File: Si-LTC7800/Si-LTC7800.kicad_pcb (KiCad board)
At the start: 2 copper layers, 40 parts, among them Q1 BSC100N06LS3_G, Q2 BSC100N06LS3_G, U1 LTC7800HUDC_PBF

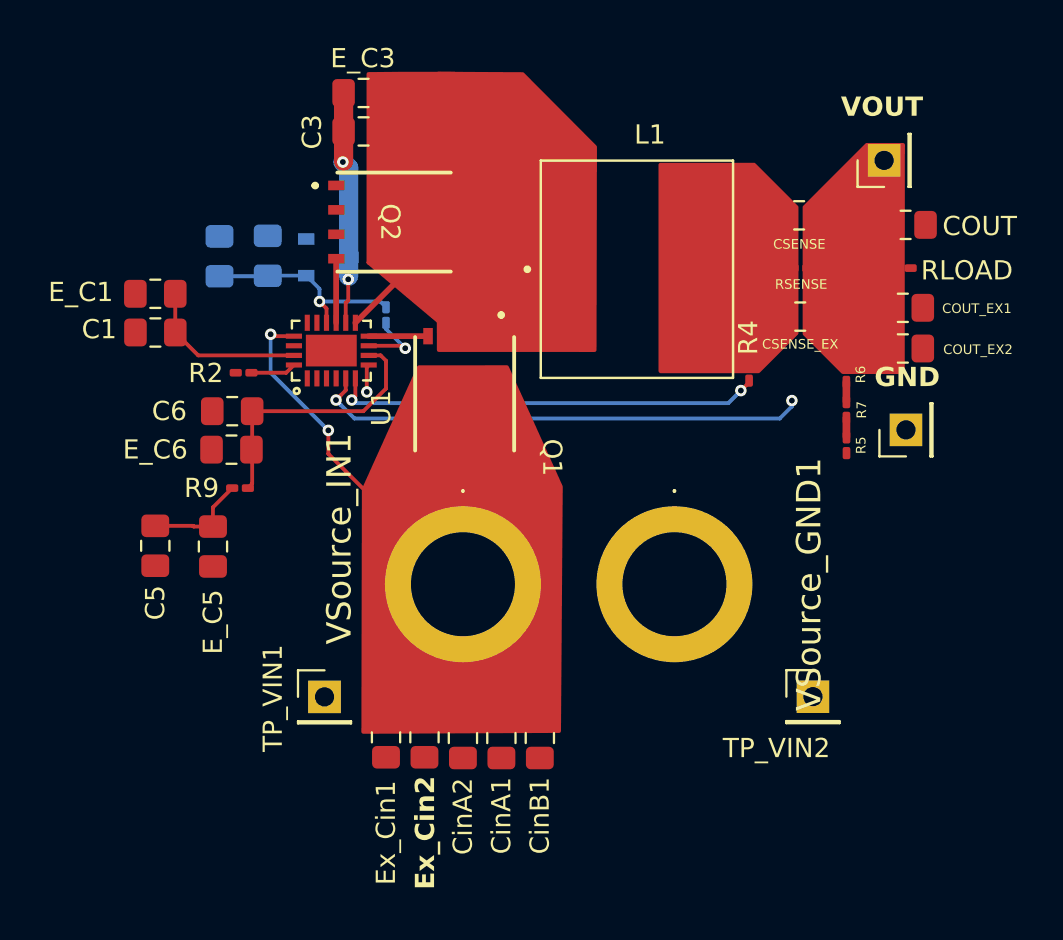
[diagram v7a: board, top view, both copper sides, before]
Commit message: Changed font size and names on PCB
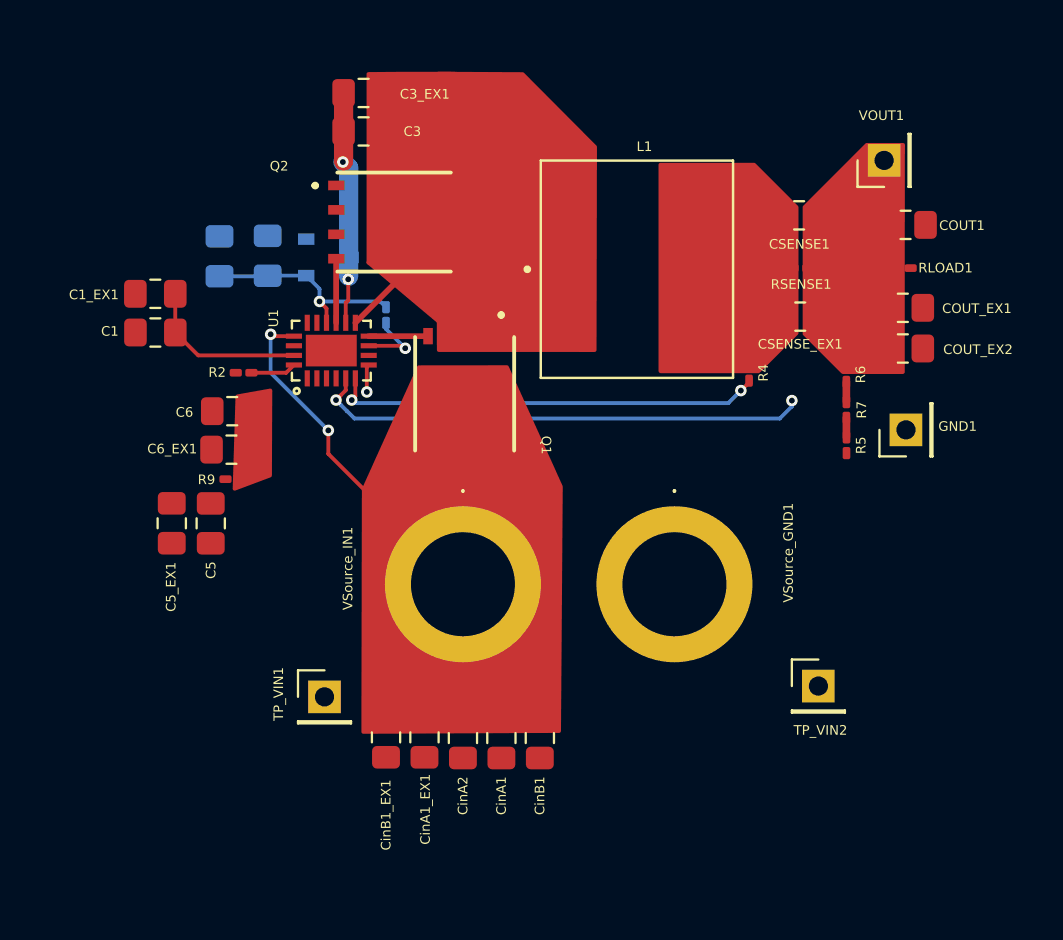
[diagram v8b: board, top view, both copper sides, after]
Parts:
- moved C5 3.11 mm to (123.9, 144.8)
- moved C5_EX1 2.46 mm to (121.9, 144.8)
- moved TP_VIN2 0.62 mm to (155.5, 153.3)
- moved R9 0.58 mm to (125.1, 142.5)
- renumbered E_C1 to C1_EX1, E_C2 to C2_EX1, E_C3 to C3_EX1, E_C5 to C5_EX1, E_C6 to C6_EX1, COUT to COUT1, CSENSE to CSENSE1, CSENSE_EX to CSENSE_EX1, Ex_Cin2 to CinA1_EX1, Ex_Cin1 to CinB1_EX1, GND to GND1, RLOAD to RLOAD1, RSENSE to RSENSE1, VOUT to VOUT1
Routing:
- net /ITH: track 14.0 -> 0.00 mm
- net Net-(C5-Pad2): track 5.43 -> 0.00 mm
